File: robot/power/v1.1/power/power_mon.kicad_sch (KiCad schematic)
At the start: 30 parts

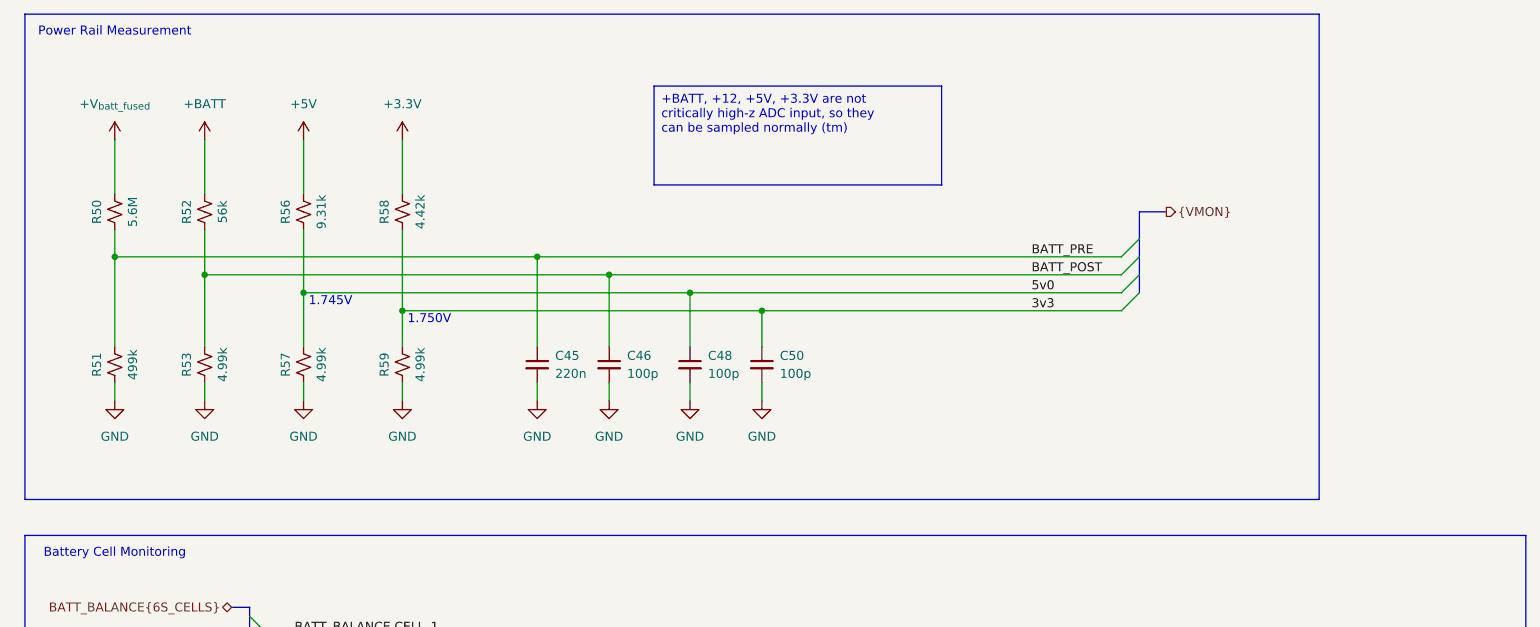
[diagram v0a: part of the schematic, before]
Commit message: power v1.1 layout work
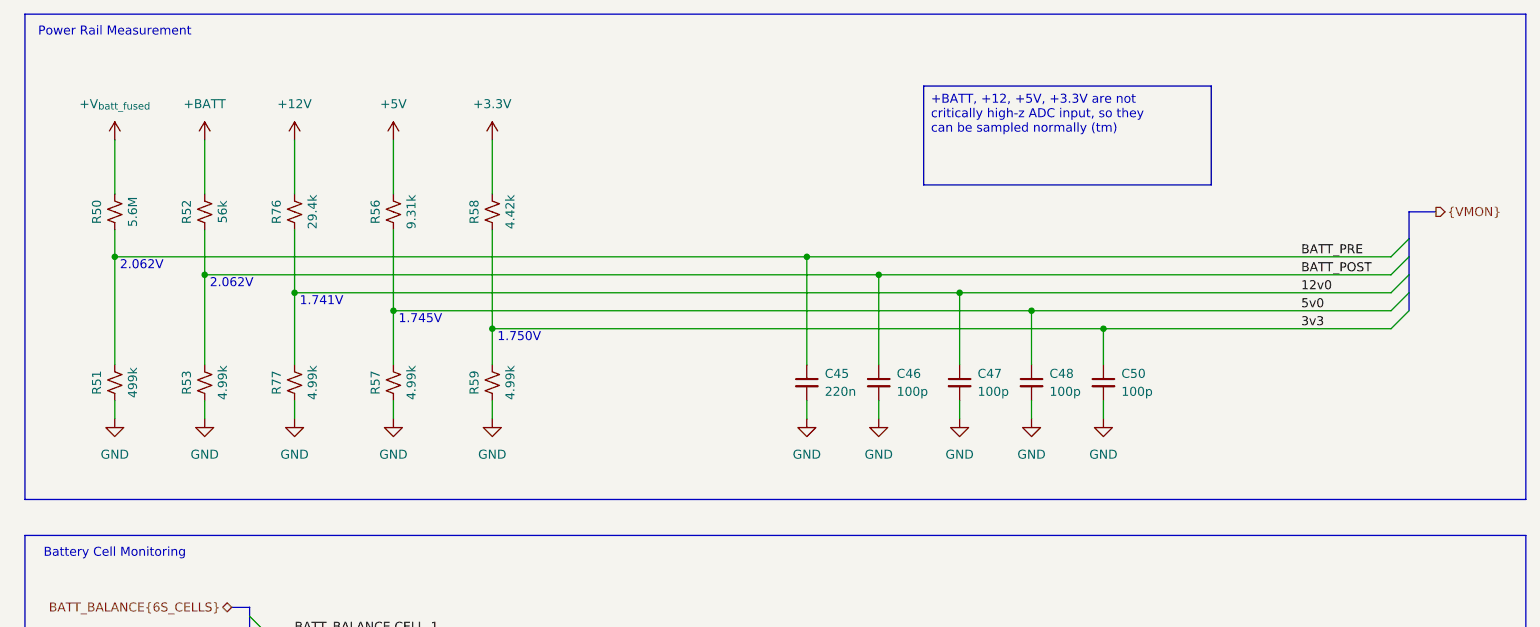
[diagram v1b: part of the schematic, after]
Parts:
- added C47: 100p, Capacitor_SMD:C_0402_1005Metric, symbol Device:C_Small
- added R76: 29.4k, Resistor_SMD:R_0402_1005Metric, symbol Device:R_Small_US
- added R77: 4.99k, Resistor_SMD:R_0402_1005Metric, symbol Device:R_Small_US
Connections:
- net GND: now also C47.2, R77.2
- new net +12V: R76.1
- new net 12v0: C47.1, R76.2, R77.1
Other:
- note added: "1.741V"
- note added: "2.062V"
- moved on the sheet: C45, C46, C48, C50, R51, R53, R56, R57, R58, R59

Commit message: power v1.1 prod files
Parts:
- C45, C49, C51, C52, C53, C54, C55: LCSC (none) -> C16772
- C46, C47, C48, C50: LCSC (none) -> C26409
- R50, R60: LCSC (none) -> C966764
- R51, R61, R63, R65, R67, R69, R71: LCSC (none) -> C25793
- R52: LCSC (none) -> C25796
- R53, R57, R59, R77: LCSC (none) -> C25903
- R56: LCSC (none) -> C270572
- R58: LCSC (none) -> C52269
- R62: LCSC (none) -> C270598
- R64: LCSC (none) -> C131575
- R66: LCSC (none) -> C477658
- R68: LCSC (none) -> C57065
- R70: LCSC (none) -> C25795
- R76: LCSC (none) -> C26973
